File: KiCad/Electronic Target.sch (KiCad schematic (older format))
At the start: 25 parts, among them J1 BERG 5x2, J2 Conn_02x04_Odd_Even, U1 LM339, U2 74HC74, U3 74HC74, U4 74HC00, U5 74LV8154, U6 74LV8154, X1 8M0

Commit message: Circuit Board Created
The first cut of the circuit board is complete.
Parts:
- removed R1: 10K0, Resistor_SMD:R_0805_2012Metric, symbol Device:R
- removed R10, R9: 220r, Resistor_SMD:R_0805_2012Metric, symbol Device:R
- removed R2: 4K7, Resistor_SMD:R_0805_2012Metric, symbol Device:R
- added C2, C3, C4, C5, C6, C7, C8: 0u1, Resistor_SMD:R_0805_2012Metric, symbol Device:C
- added R6, R7: 220r, Resistor_SMD:R_0805_2012Metric, symbol Device:R
- added RV1: 10k0, Digikey Pot:23BR10KLFTR, symbol Device:R_POT
- added TP1, TP10, TP2, TP3, TP4, TP5, TP6, TP7, TP8, TP9: TP, Connector_PinHeader_2.54mm:PinHeader_1x01_P2.54mm_Vertical, symbol Connector_Generic:Conn_01x01
- D1, D3: footprint Resistor_SMD:R_1210_3225Metric -> Resistor_SMD:R_0805_2012Metric
- D2: value GREEN -> RED; footprint Resistor_SMD:R_1210_3225Metric -> Resistor_SMD:R_0805_2012Metric
- XA1: footprint Arduino:Arduino_Mega2560_Shield -> Arduino:Arduino_Mega2560_Shield_AMB
- renumbered C2 to C9, R3 to R1, R4 to R2, R5 to R3, R6 to R4, R7 to R5
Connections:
- net GND: now also J1.7 (Pin_7), J1.9 (Pin_9), C2.2, C3.2, C4.2, C5.2, C6.2, C7.2, C8.2, RV1.3, TP10.1 (Pin_1); no longer X1.1 (EN)
- net RUN_EAST: now also TP6.1 (Pin_1)
- net RUN_NORTH: now also TP5.1 (Pin_1)
- net RUN_SOUTH: now also TP7.1 (Pin_1)
- net RUN_WEST: now also TP8.1 (Pin_1)
- net VCC: now also C2.1, C3.1, C4.1, C5.1, C6.1, C7.1, C8.1, R6.1, R7.1, RV1.1, TP9.1 (Pin_1); no longer J1.7 (Pin_7)
- net V_FB: now also RV1.2
- net at R2.2, U1.2, U2.4 (~S): now also TP1.1 (Pin_1)
- net at R3.2, U1.1, U2.10 (~S): now also TP2.1 (Pin_1)
- net at R4.2, U1.13, U3.4 (~S): now also TP3.1 (Pin_1)
- net at R5.2, U1.14, U3.10 (~S): now also TP4.1 (Pin_1)
- net QUIET: now reaches XA1.D29
- net QUIET: now also X1.1 (EN)
- net at D1.2 (A): now also R6.2; no longer R8.2
- net at D2.2 (A): now also R7.2
- net at D3.2 (A): now also R8.2
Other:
- note added: "Copyright 2020 ten-point-nine\n\nPermission is hereby granted, free of charge, to any person obtaining a copy \nof this software and associated documentation files (the "Software"), to deal\nin the Software without restriction, including without limitation the rights to \nuse, copy, modify, merge, publish, distribute, sublicense, and/or sell copies \nof the Software, and to permit persons to whom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"
- note added: "DECOUPLING CAPACITORS"

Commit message: Cleaning up documentation
Sorry, but the folders were a bit disorganized,

Cleaned up the folders and added a PDF of the schematic
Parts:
- removed J1: BERG 5x2, Connector_PinHeader_2.54mm:PinHeader_2x05_P2.54mm_Vertical, symbol Connector_Generic:Conn_2Rows-09Pins
- added C10: 10uF0, Resistor_SMD:R_1206_3216Metric, symbol Device:CP
- added J1: BERG 2x6, Connector_PinHeader_2.54mm:PinHeader_2x06_P2.54mm_Vertical, symbol Connector_Generic:Conn_2Rows-11Pins
- added unit 5 of U1
- added unit 3 of U2
- added unit 3 of U3
- added unit 5 of U4
- D1, D2, D3: footprint Resistor_SMD:R_0805_2012Metric -> Resistor_SMD:R_1210_3225Metric
- U5, U6: footprint Package_SO:SOIC-20W_7.5x12.8mm_P1.27mm -> Package_SO:TSSOP-20_4.4x6.5mm_P0.65mm
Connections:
- net GND: now also U2.11 (C), U2.12 (D), U2.2 (D), U2.3 (C), U3.11 (C), U3.12 (D), U3.2 (D), U3.3 (C), C10.2, J1.7 (Pin_7), J1.9 (Pin_9), U1.12 (V-), U2.7 (GND), U3.7 (GND), U4.7 (GND)
- net MIC_EAST: now also J1.4 (Pin_4)
- net MIC_NORTH: now also J1.2 (Pin_2)
- net MIC_SOUTH: now also J1.6 (Pin_6)
- net MIC_WEST: now also J1.8 (Pin_8)
- net VCC: now also J1.1 (Pin_1), J1.3 (Pin_3), J1.5 (Pin_5), U1.3 (V+), U2.14 (VCC), U3.14 (VCC), U4.14 (VCC)
- net at XA1.3V3 (3.3V): now also C10.1, J1.10 (Pin_10), J1.11 (Pin_11)
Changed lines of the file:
@@
 encoding utf-8
 Sheet 1 1
-Title "eTarget"
+Title "freETarget"
 Date "2020-02-16"
-Rev "AX"
-Comp "Ten_Point_Nine"
+Rev "2.0.X"
+Comp "github.com/ten-point-nine/freETarget"
 Comment1 ""
 Comment2 ""
@@
 $EndComp
 $Comp
-L Connector_Generic:Conn_2Rows-09Pins J1
-U 1 1 5E499562
-P 900 4050
-F 0 "J1" H 950 4467 50  0000 C CNN
-F 1 "BERG 5x2" H 950 4376 50  0000 C CNN
-F 2 "Connector_PinHeader_2.54mm:PinHeader_2x05_P2.54mm_Vertical" H 900 4050 50  0001 C CNN
-F 3 "~" H 900 4050 50  0001 C CNN
-	1    900  4050
-	1    0    0    -1
-$EndComp
-$Comp
 L Comparator:LM339 U1
 U 4 1 5E4A7A03
@@
 F 0 "U5" H 9950 4050 50  0000 C CNN
 F 1 "74LV8154" H 9950 3950 50  0000 C CNN
-F 2 "Package_SO:SOIC-20W_7.5x12.8mm_P1.27mm" H 9350 3800 50  0001 C CNN
+F 2 "Package_SO:TSSOP-20_4.4x6.5mm_P0.65mm" H 9350 3800 50  0001 C CNN
 F 3 "http://www.ti.com/lit/ds/symlink/sn74lv8154.pdf" H 9350 3800 50  0001 C CNN
 	1    9600 3150
@@
 F 0 "U6" H 10100 5950 50  0000 C CNN
 F 1 "74LV8154" H 10100 5850 50  0000 C CNN
-F 2 "Package_SO:SOIC-20W_7.5x12.8mm_P1.27mm" H 9350 5700 50  0001 C CNN
+F 2 "Package_SO:TSSOP-20_4.4x6.5mm_P0.65mm" H 9350 5700 50  0001 C CNN
 F 3 "http://www.ti.com/lit/ds/symlink/sn74lv8154.pdf" H 9350 5700 50  0001 C CNN
 	1    9600 5050
@@
 F 0 "D1" V 11939 2182 50  0000 R CNN
 F 1 "RED" V 11850 2200 50  0000 R CNN
-F 2 "Resistor_SMD:R_0805_2012Metric" H 11900 2300 50  0001 C CNN
+F 2 "Resistor_SMD:R_1210_3225Metric" H 11900 2300 50  0001 C CNN
 F 3 "~" H 11900 2300 50  0001 C CNN
 	1    11900 2300
@@
 F 0 "D2" V 12339 2182 50  0000 R CNN
 F 1 "RED" V 12250 2250 50  0000 R CNN
-F 2 "Resistor_SMD:R_0805_2012Metric" H 12300 2300 50  0001 C CNN
+F 2 "Resistor_SMD:R_1210_3225Metric" H 12300 2300 50  0001 C CNN
 F 3 "~" H 12300 2300 50  0001 C CNN
 	1    12300 2300
@@
 F 0 "D3" V 12739 2182 50  0000 R CNN
 F 1 "RED" V 12648 2182 50  0000 R CNN
-F 2 "Resistor_SMD:R_0805_2012Metric" H 12700 2300 50  0001 C CNN
+F 2 "Resistor_SMD:R_1210_3225Metric" H 12700 2300 50  0001 C CNN
 F 3 "~" H 12700 2300 50  0001 C CNN
 	1    12700 2300
@@
 Wire Wire Line
 	700  4250 600  4250
-Connection ~ 600  4250
 $Comp
 L power:GND #PWR02
 U 1 1 5E5FBFD2
-P 600 4450
-F 0 "#PWR02" H 600 4200 50  0001 C CNN
-F 1 "GND" H 605 4277 50  0000 C CNN
-F 2 "" H 600 4450 50  0001 C CNN
-F 3 "" H 600 4450 50  0001 C CNN
-	1    600  4450
-	1    0    0    -1
-$EndComp
-Wire Wire Line
-	600  4250 600  4450
+P 600 5100
+F 0 "#PWR02" H 600 4850 50  0001 C CNN
+F 1 "GND" H 605 4927 50  0000 C CNN
+F 2 "" H 600 5100 50  0001 C CNN
+F 3 "" H 600 5100 50  0001 C CNN
+	1    600  5100
+	1    0    0    -1
+$EndComp
+Wire Wire Line
+	600  4900 600  5100
 $Comp
 L Device:C C2
@@
 Text Notes 1050 9950 0    50   ~ 0
 Copyright 2020 ten-point-nine\n\nPermission is hereby granted, free of charge, to any person obtaining a copy \nof this software and associated documentation files (the "Software"), to deal\nin the Software without restriction, including without limitation the rights to \nuse, copy, modify, merge, publish, distribute, sublicense, and/or sell copies \nof the Software, and to permit persons to whom the Software is furnished to \ndo so, subject to the following conditions:\n\nThe above copyright notice and this permission notice shall be included in \nall copies or substantial portions of the Software.\n\nTHE SOFTWARE IS PROVIDED "AS IS", WITHOUT WARRANTY OF ANY KIND, \nEXPRESS OR IMPLIED, INCLUDING BUT NOT LIMITED TO THE WARRANTIES \nOF MERCHANTABILITY, FITNESS FOR A PARTICULAR PURPOSE AND \nNONINFRINGEMENT. IN NO EVENT SHALL THE AUTHORS OR COPYRIGHT \nHOLDERS BE LIABLE FOR ANY CLAIM, DAMAGES OR OTHER LIABILITY, \nWHETHER IN AN ACTION OF CONTRACT, TORT OR OTHERWISE, ARISING \nFROM, OUT OF OR IN CONNECTION WITH THE SOFTWARE OR THE USE \nOR OTHER DEALINGS IN THE SOFTWARE.
+$Comp
+L Connector_Generic:Conn_2Rows-11Pins J1
+U 1 1 5E60F8C1
+P 900 4050
+F 0 "J1" H 950 4467 50  0000 C CNN
+F 1 "BERG 2x6" H 950 4376 50  0000 C CNN
+F 2 "Connector_PinHeader_2.54mm:PinHeader_2x06_P2.54mm_Vertical" H 900 4050 50  0001 C CNN
+F 3 "~" H 900 4050 50  0001 C CNN
+	1    900  4050
+	1    0    0    -1
+$EndComp
+Wire Wire Line
+	15350 7150 15550 7150
+Wire Wire Line
+	15550 7150 15550 8000
+Wire Wire Line
+	15550 8000 1200 8000
+Wire Wire Line
+	700  4350 700  4450
+Wire Wire Line
+	700  4450 850  4450
+$Comp
+L Device:CP C10
+U 1 1 5E63BC82
+P 850 4750
+F 0 "C10" H 968 4796 50  0000 L CNN
+F 1 "10uF0" H 968 4705 50  0000 L CNN
+F 2 "Resistor_SMD:R_1206_3216Metric" H 888 4600 50  0001 C CNN
+F 3 "~" H 850 4750 50  0001 C CNN
+	1    850  4750
+	1    0    0    -1
+$EndComp
+Connection ~ 1200 4450
+Wire Wire Line
+	1200 4450 1200 4250
+Wire Wire Line
+	1200 4450 1200 8000
+Wire Wire Line
+	850  4900 600  4900
+Wire Wire Line
+	600  4900 600  4250
+Connection ~ 600  4900
+Connection ~ 600  4250
+Connection ~ 850  4450
+Wire Wire Line
+	850  4450 1200 4450
+Wire Wire Line
+	850  4450 850  4600
+$Comp
+L power:GND #PWR0101
+U 1 1 5E81744C
+P 4150 5950
+F 0 "#PWR0101" H 4150 5700 50  0001 C CNN
+F 1 "GND" H 4155 5777 50  0000 C CNN
+F 2 "" H 4150 5950 50  0001 C CNN
+F 3 "" H 4150 5950 50  0001 C CNN
+	1    4150 5950
+	1    0    0    -1
+$EndComp
+Wire Wire Line
+	4150 5950 4150 5800
+Wire Wire Line
+	4150 5800 4450 5800
+$Comp
+L Comparator:LM339 U1
+U 5 1 5E66D255
+P 8400 9150
+F 0 "U1" H 8358 9196 50  0000 L CNN
+F 1 "LM339" H 8358 9105 50  0000 L CNN
+F 2 "" H 8350 9250 50  0001 C CNN
+F 3 "https://www.st.com/resource/en/datasheet/lm139.pdf" H 8450 9350 50  0001 C CNN
+	5    8400 9150
+	1    0    0    -1
+$EndComp
+Wire Wire Line
+	10100 8850 10100 8750
+Wire Wire Line
+	8300 8850 8300 8750
+Wire Wire Line
+	8300 8750 9200 8750
+Wire Wire Line
+	8300 9450 8300 9750
+Wire Wire Line
+	8300 9750 9200 9750
+$Comp
+L power:VCC #PWR0102
+U 1 1 5E71100C
+P 9200 8550
+F 0 "#PWR0102" H 9200 8400 50  0001 C CNN
+F 1 "VCC" H 9215 8723 50  0000 C CNN
+F 2 "" H 9200 8550 50  0001 C CNN
+F 3 "" H 9200 8550 50  0001 C CNN
+	1    9200 8550
+	1    0    0    -1
+$EndComp
+$Comp
+L power:GND #PWR0103
+U 1 1 5E711F81
+P 9200 9900
+F 0 "#PWR0103" H 9200 9650 50  0001 C CNN
+F 1 "GND" H 9205 9727 50  0000 C CNN
+F 2 "" H 9200 9900 50  0001 C CNN
+F 3 "" H 9200 9900 50  0001 C CNN
+	1    9200 9900
+	1    0    0    -1
+$EndComp
+Wire Wire Line
+	9200 8750 9200 8550
+Connection ~ 9200 8750
+Wire Wire Line
+	9200 8750 10100 8750
+Wire Wire Line
+	9200 9750 9200 9900
+Connection ~ 9200 9750
+Wire Wire Line
+	10100 8750 11100 8750
+Connection ~ 10100 8750
+Wire Wire Line
+	9200 9750 10100 9750
+$Comp
+L 74xx:74HC74 U2
+U 3 1 5E7E0862
+P 9200 9250
+F 0 "U2" H 9430 9296 50  0000 L CNN
+F 1 "74HC74" H 9430 9205 50  0000 L CNN
+F 2 "" H 9200 9250 50  0001 C CNN
+F 3 "74xx/74hc_hct74.pdf" H 9200 9250 50  0001 C CNN
+	3    9200 9250
+	1    0    0    -1
+$EndComp
+$Comp
+L 74xx:74HC74 U3
+U 3 1 5E7E29B3
+P 10100 9250
+F 0 "U3" H 10330 9296 50  0000 L CNN
+F 1 "74HC74" H 10330 9205 50  0000 L CNN
+F 2 "" H 10100 9250 50  0001 C CNN
+F 3 "74xx/74hc_hct74.pdf" H 10100 9250 50  0001 C CNN
+	3    10100 9250
+	1    0    0    -1
+$EndComp
+$Comp
+L 74xx:74HC00 U4
+U 5 1 5E7E4AD5
+P 11100 9250
+F 0 "U4" H 11330 9296 50  0000 L CNN
+F 1 "74HC00" H 11330 9205 50  0000 L CNN
+F 2 "" H 11100 9250 50  0001 C CNN
+F 3 "http://www.ti.com/lit/gpn/sn74hc00" H 11100 9250 50  0001 C CNN
+	5    11100 9250
+	1    0    0    -1
+$EndComp
+Wire Wire Line
+	9200 8850 9200 8750
+Wire Wire Line
+	9200 9650 9200 9750
+Wire Wire Line
+	10100 9650 10100 9750
+Connection ~ 10100 9750
+Wire Wire Line
+	10100 9750 11100 9750
 $EndSCHEMATC

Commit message: Board Revisions for V2.1.X
Added traces to support calibration and setting a board revision into the software.
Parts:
- added R10, R9: 4K7, symbol Device:R
- R1: value R -> 4K7
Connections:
- net GND: now also R10.2
- net MIC_EAST: now also XA1.A2
- net MIC_NORTH: now also XA1.A1
- net MIC_SOUTH: now also XA1.A3
- net MIC_WEST: now also XA1.A4
- net VCC: now also R9.1
- net BD_REV: now reaches XA1.A5
- net BD_REV: now also R10.1, R9.2
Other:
- moved on the sheet: C1, C10, C2, C3, C4, C5, C6, C7, C8, C9, D1, D2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

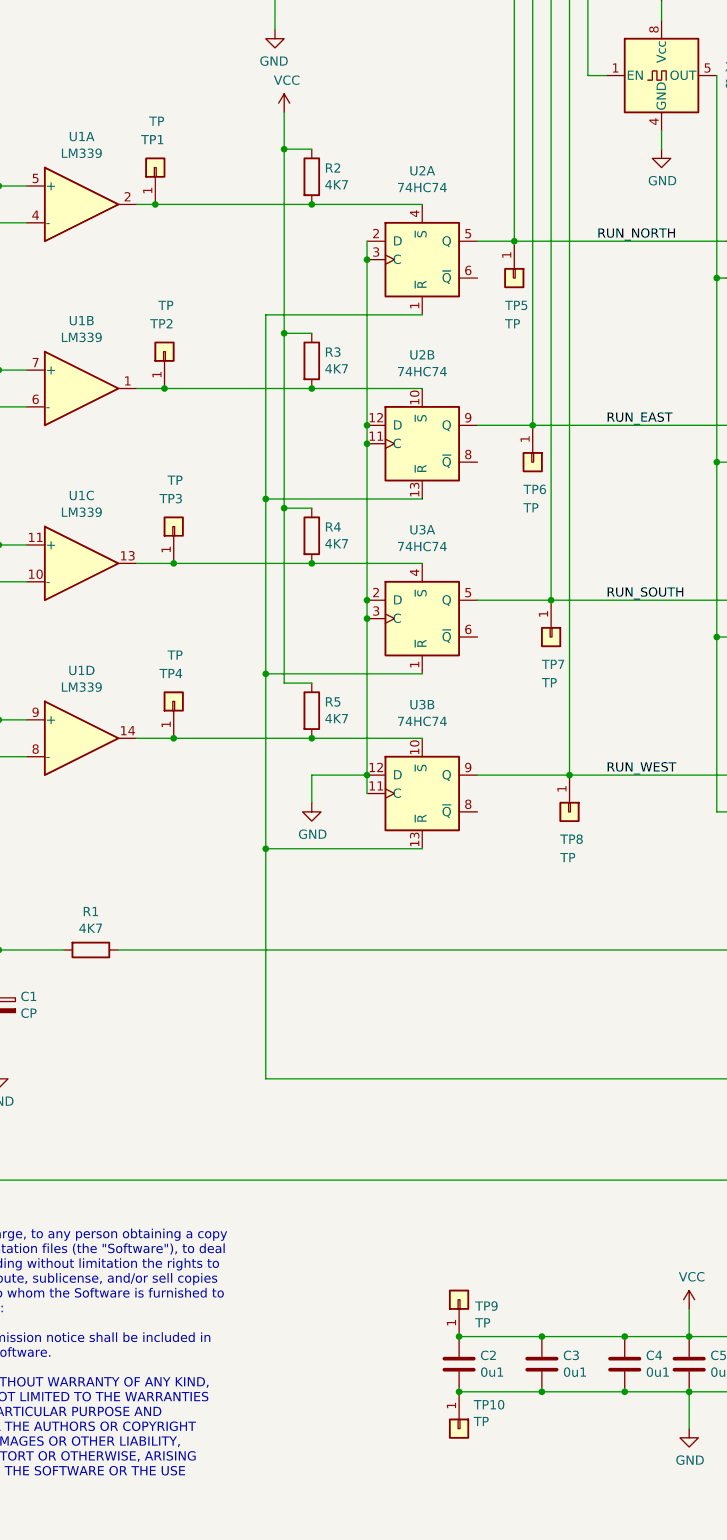
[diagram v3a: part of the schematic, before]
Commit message: Adding Interface Control Document
This details the interface between the Arduino target aquisition board and the display PC
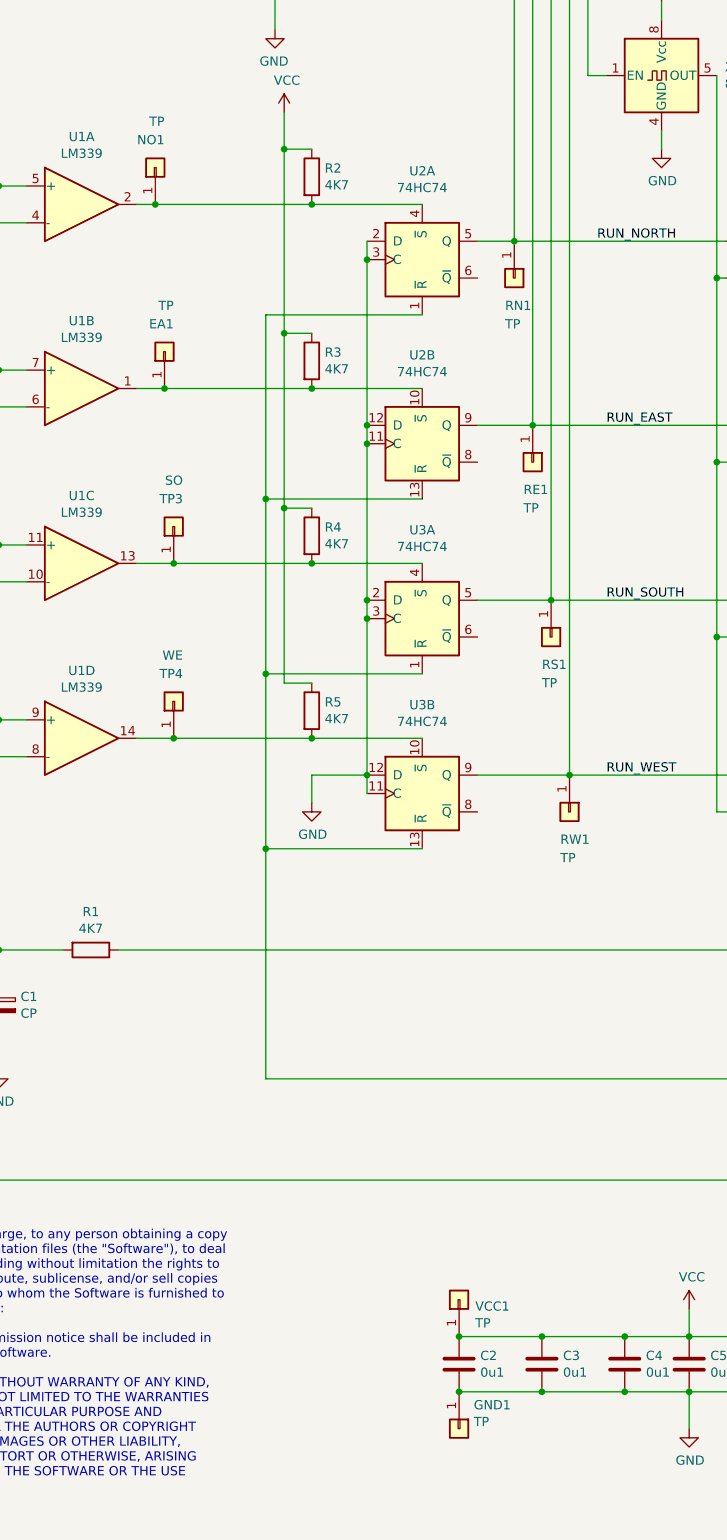
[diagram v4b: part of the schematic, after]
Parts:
- R10, R9: footprint (none) -> Resistor_SMD:R_0805_2012Metric
- TP3: value TP -> SO
- TP4: value TP -> WE
- renumbered TP2 to EA1, TP10 to GND1, TP1 to NO1, TP6 to RE1, TP5 to RN1, TP7 to RS1, TP8 to RW1, TP9 to VCC1
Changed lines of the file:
@@
 	12300 1850 12300 1700
 $Comp
-L Connector_Generic:Conn_01x01 TP10
+L Connector_Generic:Conn_01x01 GND1
 U 1 1 5E67E5A3
 P 4950 9600
-F 0 "TP10" V 4822 9680 50  0000 L CNN
+F 0 "GND1" V 4822 9680 50  0000 L CNN
 F 1 "TP" V 4913 9680 50  0000 L CNN
 F 2 "Connector_PinHeader_2.54mm:PinHeader_1x01_P2.54mm_Vertical" H 4950 9600 50  0001 C CNN
@@
 $EndComp
 $Comp
-L Connector_Generic:Conn_01x01 TP9
+L Connector_Generic:Conn_01x01 VCC1
 U 1 1 5E67FBE5
 P 4950 8900
-F 0 "TP9" V 4914 8812 50  0000 R CNN
+F 0 "VCC1" V 4914 8812 50  0000 R CNN
 F 1 "TP" V 4823 8812 50  0000 R CNN
 F 2 "Connector_PinHeader_2.54mm:PinHeader_1x01_P2.54mm_Vertical" H 4950 8900 50  0001 C CNN
@@
 $EndComp
 $Comp
-L Connector_Generic:Conn_01x01 TP5
+L Connector_Generic:Conn_01x01 RN1
 U 1 1 5E68091C
 P 5250 3350
-F 0 "TP5" V 5400 3300 50  0000 L CNN
+F 0 "RN1" V 5400 3300 50  0000 L CNN
 F 1 "TP" V 5500 3300 50  0000 L CNN
 F 2 "Connector_PinHeader_2.54mm:PinHeader_1x01_P2.54mm_Vertical" H 5250 3350 50  0001 C CNN
@@
 $EndComp
 $Comp
-L Connector_Generic:Conn_01x01 TP6
+L Connector_Generic:Conn_01x01 RE1
 U 1 1 5E6ADD2E
 P 5350 4350
-F 0 "TP6" V 5500 4300 50  0000 L CNN
+F 0 "RE1" V 5500 4300 50  0000 L CNN
 F 1 "TP" V 5600 4300 50  0000 L CNN
 F 2 "Connector_PinHeader_2.54mm:PinHeader_1x01_P2.54mm_Vertical" H 5350 4350 50  0001 C CNN
@@
 $EndComp
 $Comp
-L Connector_Generic:Conn_01x01 TP7
+L Connector_Generic:Conn_01x01 RS1
 U 1 1 5E6AED5F
 P 5450 5300
-F 0 "TP7" V 5600 5250 50  0000 L CNN
+F 0 "RS1" V 5600 5250 50  0000 L CNN
 F 1 "TP" V 5700 5250 50  0000 L CNN
 F 2 "Connector_PinHeader_2.54mm:PinHeader_1x01_P2.54mm_Vertical" H 5450 5300 50  0001 C CNN
@@
 $EndComp
 $Comp
-L Connector_Generic:Conn_01x01 TP8
+L Connector_Generic:Conn_01x01 RW1
 U 1 1 5E6AFDE2
 P 5550 6250
-F 0 "TP8" V 5700 6200 50  0000 L CNN
+F 0 "RW1" V 5700 6200 50  0000 L CNN
 F 1 "TP" V 5800 6200 50  0000 L CNN
 F 2 "Connector_PinHeader_2.54mm:PinHeader_1x01_P2.54mm_Vertical" H 5550 6250 50  0001 C CNN
@@
 P 3400 5650
 F 0 "TP4" V 3550 5600 50  0000 L CNN
-F 1 "TP" V 3650 5600 50  0000 L CNN
+F 1 "WE" V 3650 5600 50  0000 L CNN
 F 2 "Connector_PinHeader_2.54mm:PinHeader_1x01_P2.54mm_Vertical" H 3400 5650 50  0001 C CNN
 F 3 "~" H 3400 5650 50  0001 C CNN
@@
 P 3400 4700
 F 0 "TP3" V 3550 4650 50  0000 L CNN
-F 1 "TP" V 3650 4650 50  0000 L CNN
+F 1 "SO" V 3650 4650 50  0000 L CNN
 F 2 "Connector_PinHeader_2.54mm:PinHeader_1x01_P2.54mm_Vertical" H 3400 4700 50  0001 C CNN
 F 3 "~" H 3400 4700 50  0001 C CNN
@@
 	3400 4900 4150 4900
 $Comp
-L Connector_Generic:Conn_01x01 TP2
+L Connector_Generic:Conn_01x01 EA1
 U 1 1 5E6B38EB
 P 3350 3750
-F 0 "TP2" V 3500 3700 50  0000 L CNN
+F 0 "EA1" V 3500 3700 50  0000 L CNN
 F 1 "TP" V 3600 3700 50  0000 L CNN
 F 2 "Connector_PinHeader_2.54mm:PinHeader_1x01_P2.54mm_Vertical" H 3350 3750 50  0001 C CNN
@@
 	3350 3950 4150 3950
 $Comp
-L Connector_Generic:Conn_01x01 TP1
+L Connector_Generic:Conn_01x01 NO1
 U 1 1 5E6B4742
 P 3300 2750
-F 0 "TP1" V 3450 2700 50  0000 L CNN
+F 0 "NO1" V 3450 2700 50  0000 L CNN
 F 1 "TP" V 3550 2700 50  0000 L CNN
 F 2 "Connector_PinHeader_2.54mm:PinHeader_1x01_P2.54mm_Vertical" H 3300 2750 50  0001 C CNN
@@
 F 0 "R9" H 16120 5746 50  0000 L CNN
 F 1 "4K7" H 16120 5655 50  0000 L CNN
-F 2 "" V 15980 5700 50  0001 C CNN
+F 2 "Resistor_SMD:R_0805_2012Metric" V 15980 5700 50  0001 C CNN
 F 3 "~" H 16050 5700 50  0001 C CNN
 	1    16050 5700
@@
 F 0 "R10" H 16120 6146 50  0000 L CNN
 F 1 "4K7" H 16120 6055 50  0000 L CNN
-F 2 "" V 15980 6100 50  0001 C CNN
+F 2 "Resistor_SMD:R_0805_2012Metric" V 15980 6100 50  0001 C CNN
 F 3 "~" H 16050 6100 50  0001 C CNN
 	1    16050 6100
